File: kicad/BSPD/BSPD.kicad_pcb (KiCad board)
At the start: 2 copper layers, 57 x 50 mm, 59 parts, among them J1 Conn_01x02, J2 Conn_01x02, J3 Conn_01x02, K1 SANYOU_SRD_Form_C, Q1 AO3400A, Q2 AO3401A, Q3 AO3400A, U1 LM393, U2 LM393, U3 74AHC1G00, U4 74AHC1G00, U5 LM78M05_TO252, U6 LM393, U7 LM393

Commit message: minor fix
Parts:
- added F1: Fuse, Fuse:Fuse_0805_2012Metric_Pad1.15x1.40mm_HandSolder, B.Cu at (173.9, 76.4)
- added R26: 10k, Resistor_SMD:R_0805_2012Metric_Pad1.20x1.40mm_HandSolder, F.Cu at (172.7, 83.8)
- added R27: 10k, Resistor_SMD:R_0805_2012Metric_Pad1.20x1.40mm_HandSolder, F.Cu at (171.9, 88.2)
- added R28: 100k, Resistor_SMD:R_0805_2012Metric_Pad1.20x1.40mm_HandSolder, F.Cu at (171.9, 90.3)
- added R29: 100k, Resistor_SMD:R_0805_2012Metric_Pad1.20x1.40mm_HandSolder, F.Cu at (171.8, 80.8)
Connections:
- J1 pad 1: /SIGN2 -> Net-(J1-Pin_1)
- J1 pad 2: /SIGN1 -> Net-(J1-Pin_2)
- J3 pad 1: +12V -> Net-(J3-Pin_1)
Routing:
- net +5V: track 175.9 -> 169.4 mm
- net Net-(J1-Pin_2): track 0.00 -> 4.85 mm
- net Net-(J1-Pin_1): track 0.00 -> 4.50 mm
- net /SIGN2: track 59.4 -> 57.1 mm
- net /SIGN1: track 42.6 -> 40.7 mm
- net GND: track 11.5 -> 10.8 mm, vias 111 -> 126
- added copper zone on B.Cu, net Net-(J3-Pin_1)

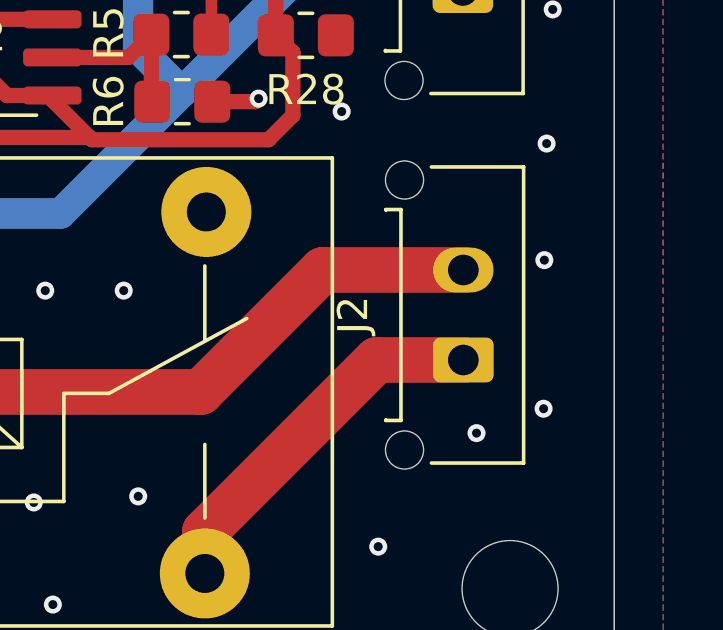
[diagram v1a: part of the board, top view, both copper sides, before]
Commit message: added silkscreen
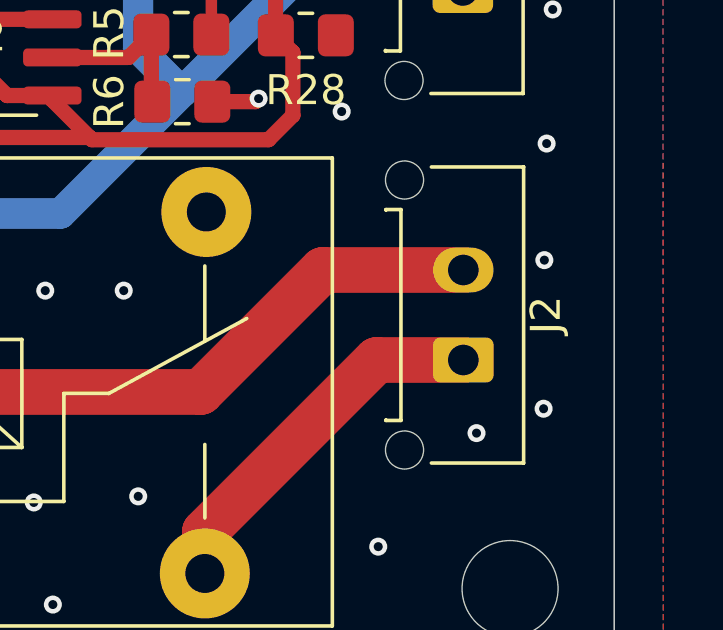
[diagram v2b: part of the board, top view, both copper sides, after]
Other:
- board text added: "12V"
- board text added: "GND"
- board text added: "SC1"
- board text added: "SC2"
- board text added: "SIG1"
- board text added: "SIG2"
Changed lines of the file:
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@@
 		(tags "connector Molex Micro-Fit_3.0 vertical")
 		(property "Reference" "J2"
-			(at 1.5 -3.67 90)
+			(at 1.5 2.7518 90)
 			(layer "F.SilkS")
 			(effects
@@
 		(layer "Edge.Cuts")
 	)
+	(gr_text "GND"
+		(at 180.467 71.5518 90)
+		(layer "B.SilkS")
+		(effects
+			(font
+				(size 1 1)
+				(thickness 0.1)
+			)
+			(justify left bottom mirror)
+		)
+	)
+	(gr_text "SIG1"
+		(at 180.4162 83.4898 90)
+		(layer "B.SilkS")
+		(effects
+			(font
+				(size 1 1)
+				(thickness 0.1)
+			)
+			(justify left bottom mirror)
+		)
+	)
+	(gr_text "12V"
+		(at 180.4924 75.3872 90)
+		(layer "B.SilkS")
+		(effects
+			(font
+				(size 1 1)
+				(thickness 0.1)
+			)
+			(justify left bottom mirror)
+		)
+	)
+	(gr_text "SC1"
+		(at 180.6194 96.6216 90)
+		(layer "B.SilkS")
+		(effects
+			(font
+				(size 1 1)
+				(thickness 0.1)
+			)
+			(justify left bottom mirror)
+		)
+	)
+	(gr_text "SIG2"
+		(at 180.4162 87.5538 90)
+		(layer "B.SilkS")
+		(effects
+			(font
+				(size 1 1)
+				(thickness 0.1)
+			)
+			(justify left bottom mirror)
+		)
+	)
+	(gr_text "SC2"
+		(at 180.6448 100.0252 90)
+		(layer "B.SilkS")
+		(effects
+			(font
+				(size 1 1)
+				(thickness 0.1)
+			)
+			(justify left bottom mirror)
+		)
+	)
 	(via

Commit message: minor update
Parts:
- moved C4 1.38 mm to (162.1, 73.8)
- moved C1 0.33 mm to (165.2, 75.4), turned to -135 degrees
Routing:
- net +5V: track 169.4 -> 173.9 mm
- net GND: vias 126 -> 135
- net (no net): vias 1 -> 0
